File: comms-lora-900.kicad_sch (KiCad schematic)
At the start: 11 parts, among them J1 Conn_Coaxial_Small, U4 RFM95W-915S2

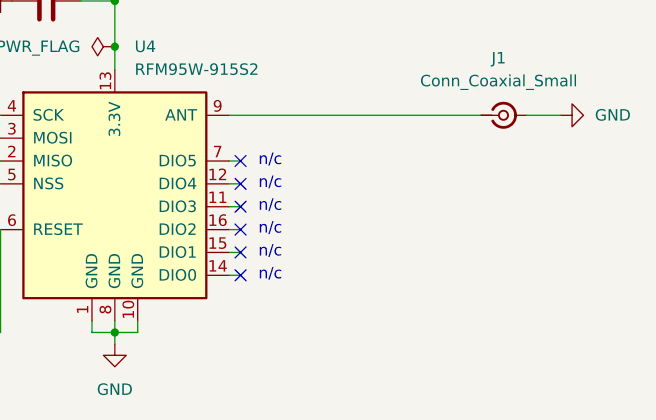
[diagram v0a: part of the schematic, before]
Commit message: Added mounting holes
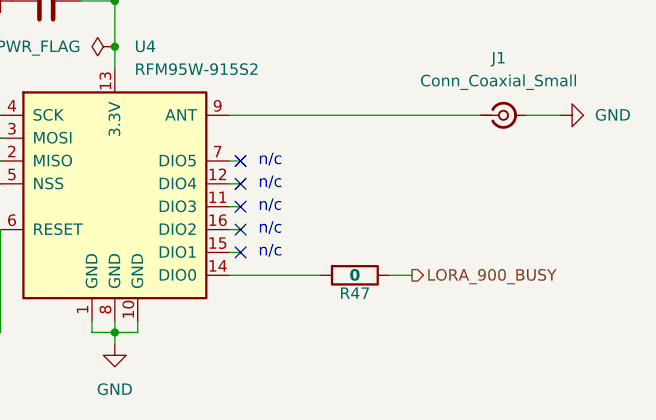
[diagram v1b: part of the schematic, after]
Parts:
- added R47: 0, Resistor_SMD:R_0603_1608Metric, symbol Device:R
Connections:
- net at U4.14 (DIO0): now also R47.2
- new net LORA_900_BUSY: R47.1
- no-connect marks 6 -> 5
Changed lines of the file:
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@@
-	)
-	(no_connect
-		(at 158.75 107.95)
 	)
 	(no_connect
@@
 	(wire
 		(pts
+			(xy 175.26 107.95) (xy 177.8 107.95)
+		)
+		(stroke
+			(width 0)
+			(type default)
+		)
+	)
+	(wire
+		(pts
 			(xy 157.48 100.33) (xy 158.75 100.33)
 		)
@@
 	(wire
 		(pts
-			(xy 157.48 107.95) (xy 158.75 107.95)
+			(xy 157.48 107.95) (xy 167.64 107.95)
 		)
 		(stroke
@@
 		(exclude_from_sim no)
 		(at 162.052 105.41 0)
-		(effects
-			(font
-				(size 1.27 1.27)
-			)
-		)
-	)
-	(text "n/c"
-		(exclude_from_sim no)
-		(at 162.052 107.95 0)
 		(effects
 			(font
@@
 			)
 			(justify right)
+		)
+	)
+	(hierarchical_label "LORA_900_BUSY"
+		(shape output)
+		(at 177.8 107.95 0)
+		(fields_autoplaced yes)
+		(effects
+			(font
+				(size 1.27 1.27)
+			)
+			(justify left)
 		)
 	)
@@
 					(unit 1)
 				)
+			)
+		)
+	)
+	(symbol
+		(lib_id "Device:R")
+		(at 171.45 107.95 270)
+		(unit 1)
+		(exclude_from_sim no)
+		(in_bom yes)
+		(on_board yes)
+		(dnp no)
+		(property "Reference" "R47"
+			(at 171.45 109.982 90)
+			(effects
+				(font
+					(size 1.27 1.27)
+				)
+			)
+		)
+		(property "Value" "0"
+			(at 171.45 107.95 90)
+			(effects
+				(font
+					(size 1.27 1.27)
+					(thickness 0.254)
+					(bold yes)
+				)
+			)
+		)
+		(property "Footprint" "Resistor_SMD:R_0603_1608Metric"
+			(at 171.45 106.172 90)
+			(effects
+				(font
+					(size 1.27 1.27)
+				)
+				(hide yes)
+			)
+		)
+		(property "Datasheet" "Datasheet"
+			(at 171.45 107.95 0)
+			(effects
+				(font
+					(size 1.27 1.27)
+				)
+				(hide yes)
+			)
+		)
+		(property "Description" "Resistor"
+			(at 171.45 107.95 0)
+			(effects
+				(font
+					(size 1.27 1.27)
+				)
+				(hide yes)
+			)
+		)
+		(property "Mfr" "YAGEO"
+			(at 171.45 107.95 0)
+			(effects
+				(font
+					(size 1.27 1.27)
+				)
+				(hide yes)
+			)
+		)
+		(property "Mfr P/N" "RC0603JR-070RL"
+			(at 171.45 107.95 0)
+			(effects
+				(font
+					(size 1.27 1.27)
+				)
+				(hide yes)
+			)
+		)
+		(property "Supplier_1" "Digikey"
+			(at 171.45 107.95 0)
+			(effects
+				(font
+					(size 1.27 1.27)
+				)
+				(hide yes)
+			)
+		)
+		(property "Supplier_1 P/N" "311-0.0GRCT-ND"
+			(at 171.45 107.95 0)
+			(effects
+				(font
+					(size 1.27 1.27)
+				)
+				(hide yes)
+			)
+		)
+		(property "Supplier_1 Unit Price" "$0.10000 "
+			(at 171.45 107.95 0)
+			(effects
+				(font
+					(size 1.27 1.27)
+				)
+				(hide yes)
+			)
+		)
+		(property "Supplier_1 Price @ Qty" "$0.00304 "
+			(at 171.45 107.95 0)
+			(effects
+				(font
+					(size 1.27 1.27)
+				)
+				(hide yes)
+			)
+		)
+		(property "Supplier_2" ""
+			(at 171.45 107.95 0)
+			(effects
+				(font
+					(size 1.27 1.27)
+				)
+				(hide yes)
+			)
+		)
+		(property "Supplier_2 P/N" ""
+			(at 171.45 107.95 0)
+			(effects
+				(font
+					(size 1.27 1.27)
+				)
+				(hide yes)
+			)
+		)
+		(property "Supplier_2 Unit Price" ""
+			(at 171.45 107.95 0)
+			(effects
+				(font
+					(size 1.27 1.27)
+				)
+				(hide yes)
+			)
+		)
+		(property "Supplier_2 Price @ Qty" ""
+			(at 171.45 107.95 0)
+			(effects
+				(font
+					(size 1.27 1.27)
+				)
+				(hide yes)
+			)
+		)
+		(pin "1"
+		)
+		(pin "2"
+		)
+		(instances
+			(project "roamer"
+				(path "/1c59de6a-87fe-4223-8898-4b0383164a31/74b4b058-6b85-4b9e-95dc-72d767f949d9"
+					(reference "R47")
+					(unit 1)
+				)

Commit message: Creating fab package
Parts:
- J1: Supplier_1 Price @ Qty $0.38945 -> 0.38945; Supplier_1 Unit Price $0.94000 -> 0.94000
- R10, R11, R22, R33, R35, R37, R47: Supplier_1 Price @ Qty $0.00304 -> 0.00304; Supplier_1 Unit Price $0.10000 -> 0.10000
- U4: Mfr Adafruit -> Adafruit Industries LLC; Supplier_1 Supplier_1 P/N 0 0 Center Center 0 0 -> Digikey; Supplier_1 P/N 3072 -> 1528-1667-ND; Supplier_1 Price @ Qty $15.96 -> 19.95000; Supplier_1 Unit Price $19.95 -> 19.95000
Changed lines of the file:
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@@
 			)
 		)
-		(property "Supplier_1 Unit Price" "$0.10000 "
+		(property "Supplier_1 Unit Price" "0.10000 "
 			(at 123.19 90.17 0)
 			(effects
@@
 			)
 		)
-		(property "Supplier_1 Price @ Qty" "$0.00304 "
+		(property "Supplier_1 Price @ Qty" "0.00304 "
 			(at 123.19 90.17 0)
 			(effects
@@
 			)
 		)
-		(property "Supplier_1 Unit Price" "$0.10000 "
+		(property "Supplier_1 Unit Price" "0.10000 "
 			(at 123.19 114.3 0)
 			(effects
@@
 			)
 		)
-		(property "Supplier_1 Price @ Qty" "$0.00304 "
+		(property "Supplier_1 Price @ Qty" "0.00304 "
 			(at 123.19 114.3 0)
 			(effects
@@
 			)
 		)
-		(property "Supplier_1 Unit Price" "$0.10000 "
+		(property "Supplier_1 Unit Price" "0.10000 "
 			(at 123.19 95.25 0)
 			(effects
@@
 			)
 		)
-		(property "Supplier_1 Price @ Qty" "$0.00304 "
+		(property "Supplier_1 Price @ Qty" "0.00304 "
 			(at 123.19 95.25 0)
 			(effects
@@
 			)
 		)
-		(property "Supplier_1 Unit Price" "$0.10000 "
+		(property "Supplier_1 Unit Price" "0.10000 "
 			(at 144.78 68.58 0)
 			(effects
@@
 			)
 		)
-		(property "Supplier_1 Price @ Qty" "$0.00304 "
+		(property "Supplier_1 Price @ Qty" "0.00304 "
 			(at 144.78 68.58 0)
 			(effects
@@
 			)
 		)
-		(property "Supplier_1 Unit Price" "$0.10000 "
+		(property "Supplier_1 Unit Price" "0.10000 "
 			(at 123.19 92.71 0)
 			(effects
@@
 			)
 		)
-		(property "Supplier_1 Price @ Qty" "$0.00304 "
+		(property "Supplier_1 Price @ Qty" "0.00304 "
 			(at 123.19 92.71 0)
 			(effects
@@
 			)
 		)
-		(property "Mfr" "Adafruit"
+		(property "Mfr" "Adafruit Industries LLC"
 			(at 144.78 97.79 0)
 			(effects
@@
 			)
 		)
-		(property "Supplier_1" "Supplier_1 P/N  0 0 Center Center 0 0  "
+		(property "Supplier_1" "Digikey"
 			(at 144.78 97.79 0)
 			(effects
@@
 			)
 		)
-		(property "Supplier_1 P/N" "3072"
+		(property "Supplier_1 P/N" "1528-1667-ND"
 			(at 144.78 97.79 0)
 			(effects
@@
 			)
 		)
-		(property "Supplier_1 Unit Price" "$19.95"
+		(property "Supplier_1 Unit Price" "19.95000"
 			(at 144.78 97.79 0)
 			(effects
@@
 			)
 		)
-		(property "Supplier_1 Price @ Qty" "$15.96"
+		(property "Supplier_1 Price @ Qty" "19.95000"
 			(at 144.78 97.79 0)
 			(effects
@@
 			)
 		)
-		(property "Supplier_1 Unit Price" "$0.10000 "
+		(property "Supplier_1 Unit Price" "0.10000 "
 			(at 171.45 107.95 0)
 			(effects
@@
 			)
 		)
-		(property "Supplier_1 Price @ Qty" "$0.00304 "
+		(property "Supplier_1 Price @ Qty" "0.00304 "
 			(at 171.45 107.95 0)
 			(effects
@@
 			)
 		)
-		(property "Supplier_1 Unit Price" "$0.10000 "
+		(property "Supplier_1 Unit Price" "0.10000 "
 			(at 123.19 99.06 0)
 			(effects
@@
 			)
 		)
-		(property "Supplier_1 Price @ Qty" "$0.00304 "
+		(property "Supplier_1 Price @ Qty" "0.00304 "
 			(at 123.19 99.06 0)
 			(effects
@@
 			)
 		)
-		(property "Supplier_1 Unit Price" "$0.94000 "
+		(property "Supplier_1 Unit Price" "0.94000 "
 			(at 187.96 90.17 0)
 			(effects
@@
 			)
 		)
-		(property "Supplier_1 Price @ Qty" "$0.38945 "
+		(property "Supplier_1 Price @ Qty" "0.38945 "
 			(at 187.96 90.17 0)
 			(effects

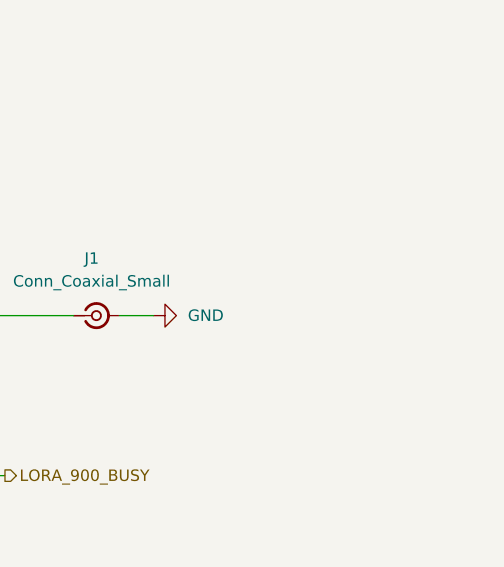
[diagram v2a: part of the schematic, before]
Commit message: Updating silkscreen comments
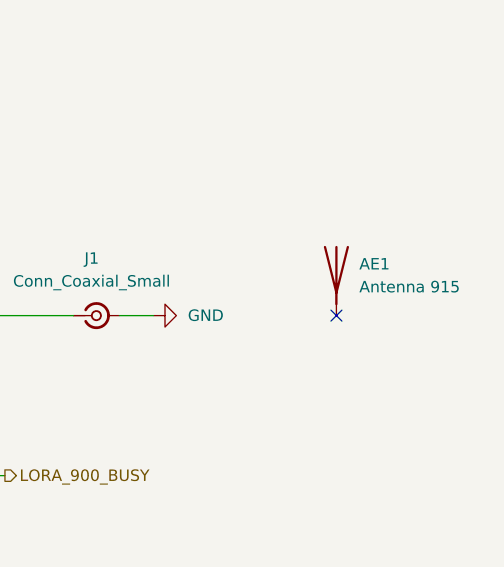
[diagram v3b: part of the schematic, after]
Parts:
- added AE1: Antenna 915, symbol Device:Antenna
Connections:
- no-connect marks 5 -> 6
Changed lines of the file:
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@@
+	)
+	(no_connect
+		(at 214.63 90.17)
 	)
 	(no_connect
@@
 					(unit 1)
 				)
+			)
+		)
+	)
+	(symbol
+		(lib_id "Device:Antenna")
+		(at 214.63 85.09 0)
+		(unit 1)
+		(exclude_from_sim no)
+		(in_bom yes)
+		(on_board yes)
+		(dnp no)
+		(fields_autoplaced yes)
+		(property "Reference" "AE1"
+			(at 217.17 84.4549 0)
+			(effects
+				(font
+					(size 1.27 1.27)
+				)
+				(justify left)
+			)
+		)
+		(property "Value" "Antenna 915"
+			(at 217.17 86.9949 0)
+			(effects
+				(font
+					(size 1.27 1.27)
+				)
+				(justify left)
+			)
+		)
+		(property "Footprint" ""
+			(at 214.63 85.09 0)
+			(effects
+				(font
+					(size 1.27 1.27)
+				)
+				(hide yes)
+			)
+		)
+		(property "Datasheet" "RF ANT 916MHZ WHIP STR CAB PAN"
+			(at 214.63 85.09 0)
+			(effects
+				(font
+					(size 1.27 1.27)
+				)
+				(hide yes)
+			)
+		)
+		(property "Description" "Antenna"
+			(at 214.63 85.09 0)
+			(effects
+				(font
+					(size 1.27 1.27)
+				)
+				(hide yes)
+			)
+		)
+		(property "Mfr" "TE Connectivity Linx"
+			(at 214.63 85.09 0)
+			(effects
+				(font
+					(size 1.27 1.27)
+				)
+				(hide yes)
+			)
+		)
+		(property "Mfr P/N" "ANT-916-PW-QW-UFL"
+			(at 214.63 85.09 0)
+			(effects
+				(font
+					(size 1.27 1.27)
+				)
+				(hide yes)
+			)
+		)
+		(property "Supplier_1" "DigiKey"
+			(at 214.63 85.09 0)
+			(effects
+				(font
+					(size 1.27 1.27)
+				)
+				(hide yes)
+			)
+		)
+		(property "Supplier_1 P/N" "ANT-916-PW-QW-UFL-ND"
+			(at 214.63 85.09 0)
+			(effects
+				(font
+					(size 1.27 1.27)
+				)
+				(hide yes)
+			)
+		)
+		(property "Supplier_1 Unit Price" "9.48000"
+			(at 214.63 85.09 0)
+			(effects
+				(font
+					(size 1.27 1.27)
+				)
+				(hide yes)
+			)
+		)
+		(property "Supplier_1 Price @ Qty" ""
+			(at 214.63 85.09 0)
+			(effects
+				(font
+					(size 1.27 1.27)
+				)
+				(hide yes)
+			)
+		)
+		(property "Supplier_2" ""
+			(at 214.63 85.09 0)
+			(effects
+				(font
+					(size 1.27 1.27)
+				)
+				(hide yes)
+			)
+		)
+		(property "Supplier_2 P/N" ""
+			(at 214.63 85.09 0)
+			(effects
+				(font
+					(size 1.27 1.27)
+				)
+				(hide yes)
+			)
+		)
+		(property "Supplier_2 Unit Price" ""
+			(at 214.63 85.09 0)
+			(effects
+				(font
+					(size 1.27 1.27)
+				)
+				(hide yes)
+			)
+		)
+		(property "Supplier_2 Price @ Qty" ""
+			(at 214.63 85.09 0)
+			(effects
+				(font
+					(size 1.27 1.27)
+				)
+				(hide yes)
+			)
+		)
+		(pin "1"
+		)
+		(instances
+			(project ""
+				(path "/1c59de6a-87fe-4223-8898-4b0383164a31/74b4b058-6b85-4b9e-95dc-72d767f949d9"
+					(reference "AE1")
+					(unit 1)
+				)
